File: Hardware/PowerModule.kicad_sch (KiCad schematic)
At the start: 27 parts, among them U2 LM2596S-5, U3 LM1117-3.3, U4 LM1117-3.3, U5 LM1117-3.3

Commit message: Deleted 24V section
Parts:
- removed C10: 100nF, Capacitor_SMD:C_0603_1608Metric_Pad1.08x0.95mm_HandSolder, symbol Device:C
- removed C11: 220u, Capacitor_SMD:CP_Elec_6.3x7.7, symbol Device:CP1
- removed C21, C22: C_Small, Capacitor_SMD:C_0603_1608Metric_Pad1.08x0.95mm_HandSolder, symbol Device:C_Small
- removed C9: 100u, Capacitor_SMD:CP_Elec_6.3x7.7, symbol Device:CP1
- removed D4: 30V, Diode_SMD:D_SMB, symbol Device:D_Zener
- removed D5: Fast diode, Diode_SMD:D_SMB, symbol Device:D_Schottky
- removed D6: D_Schottky, Diode_SMD:D_SMB, symbol Device:D_Schottky
- removed D7, D8: LED, LED_SMD:LED_0603_1608Metric_Pad1.05x0.95mm_HandSolder, symbol Device:LED
- removed F1: 500mA, Fuse:Fuse_2010_5025Metric, symbol Device:Polyfuse
- removed FB1: Ferrite_Bead_Small, Inductor_SMD:L_0805_2012Metric, symbol Device:Ferrite_Bead_Small
- removed L2: 33u, Inductor_SMD:L_12x12mm_H8mm, symbol Device:L
- removed R6: 4k7R, Resistor_SMD:R_0603_1608Metric_Pad0.98x0.95mm_HandSolder, symbol Device:R
- removed R7: 680R, Resistor_SMD:R_0603_1608Metric_Pad0.98x0.95mm_HandSolder, symbol Device:R
- removed U2: LM2596S-5, Package_TO_SOT_SMD:TO-263-5_TabPin3, symbol Regulator_Switching:LM2596S-5
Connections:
- net 3V3_POT1: now also C15.1, F2.2, U4.2 (VO)
- net 3V3_POT2: now also C17.1, F3.2, U5.2 (VO)

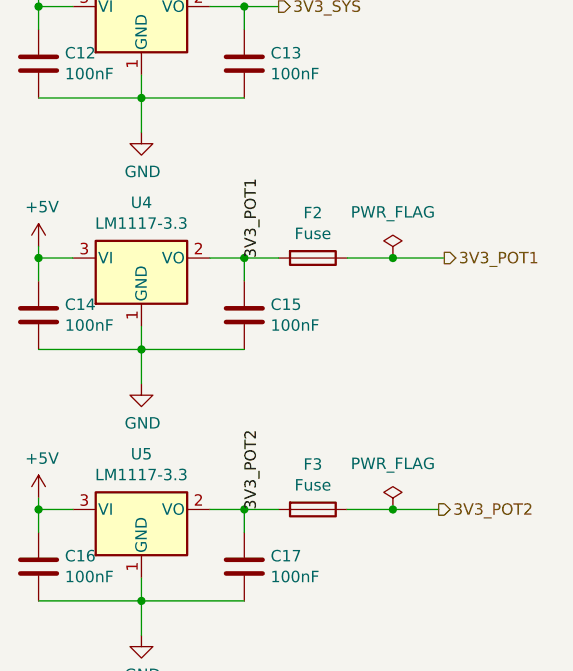
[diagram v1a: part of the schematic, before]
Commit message: Changed crystal footprint, fixed capactiors, added debug LED
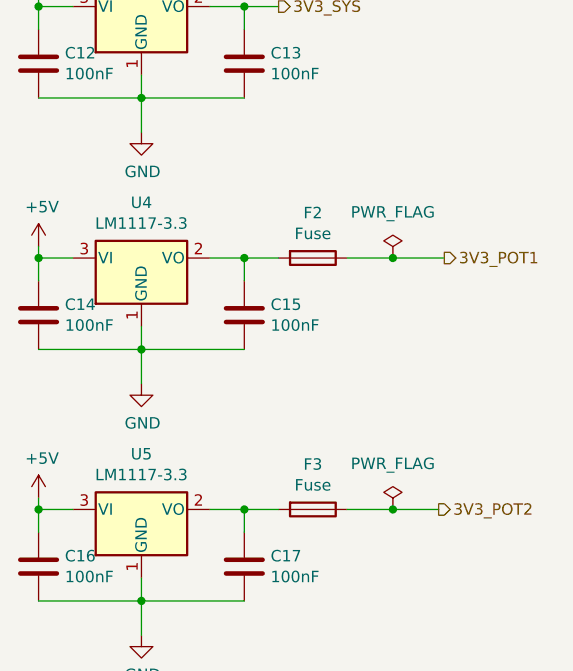
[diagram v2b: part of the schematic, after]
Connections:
- net 3V3_POT1: no longer C15.1, F2.2, U4.2 (VO)
- net 3V3_POT2: no longer C17.1, F3.2, U5.2 (VO)
- new net: C15.1, F2.2, U4.2 (VO)
- new net: C17.1, F3.2, U5.2 (VO)
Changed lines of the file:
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@@
     (stroke (width 0) (type default) (color 0 0 0 0))
-  )
-  (label "3V3_POT2" (at 147.828 147.32 90)
-    (effects (font (size 1.27 1.27)) (justify left bottom))
-  )
-  (label "3V3_POT1" (at 147.828 119.38 90)
-    (effects (font (size 1.27 1.27)) (justify left bottom))
   )
   (hierarchical_label "3V3_POT1" (shape output) (at 168.275 119.38 0)

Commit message: Schematic cleanup
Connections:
- net VO_POT1: now reaches C15.1, F2.2, U4.2 (VO)
- net VO_POT2: now reaches C17.1, F3.2, U5.2 (VO)
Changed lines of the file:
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@@
     (stroke (width 0) (type default) (color 0 0 0 0))
+  )
+  (label "VO_POT1" (at 142.748 119.38 0)
+    (effects (font (size 1.27 1.27)) (justify left bottom))
+  )
+  (label "VO_POT2" (at 142.494 147.32 0)
+    (effects (font (size 1.27 1.27)) (justify left bottom))
   )
   (hierarchical_label "3V3_POT1" (shape output) (at 168.275 119.38 0)
